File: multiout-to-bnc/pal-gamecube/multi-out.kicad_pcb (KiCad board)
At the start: 2 copper layers, 18.4 x 12 mm, 16 parts, among them U1 AV-CONNECTOR, U2 LM1881

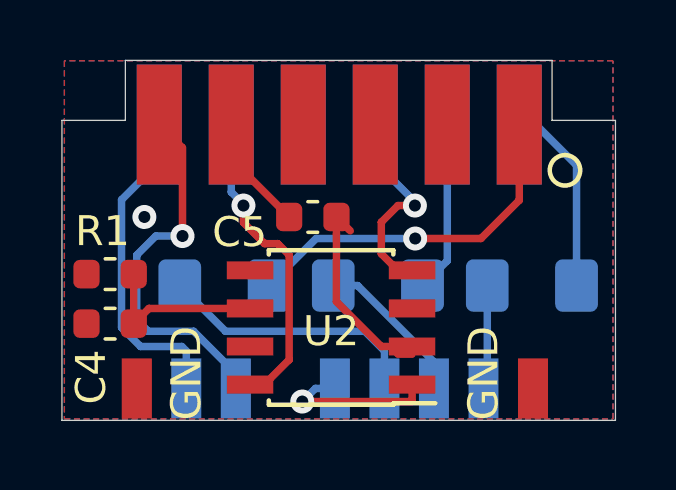
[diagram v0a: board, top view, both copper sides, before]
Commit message: Add 75 Ohm resistor between composite line and ground
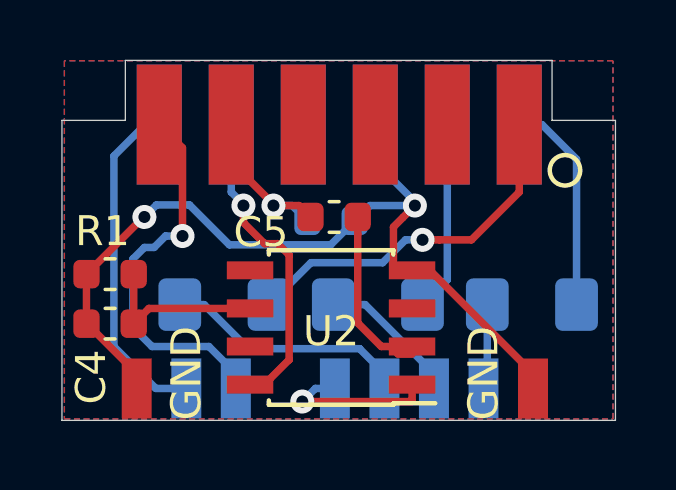
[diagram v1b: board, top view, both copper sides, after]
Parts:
- added R2: 75k, Resistor_SMD:R_0603_1608Metric, B.Cu at (149.0, 109.3)
- moved C5 0.71 mm to (149.1, 109.2)
- moved C1 0.64 mm to (145.4, 112.1)
- moved C2 0.64 mm to (155.7, 112.1)
- moved C3 0.64 mm to (150.5, 112.1)
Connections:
- U1 pad 3: (no net) -> Net-(U1-Pad3)
- U1 pad 7: (no net) -> Net-(U1-Pad7)
- U1 pad 8: (no net) -> Net-(U1-Pad8)
- U2 pad 3: (no net) -> Net-(U2-Pad3)
- U2 pad 5: (no net) -> Net-(U2-Pad5)
- U2 pad 7: (no net) -> Net-(U2-Pad7)
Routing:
- net GND: track 6.90 -> 29.7 mm
- net Net-(C1-Pad1): track 13.3 -> 12.1 mm
- net Net-(C5-Pad2): track 7.09 -> 6.14 mm
- net Net-(C5-Pad1): track 5.13 -> 6.02 mm, vias 0 -> 1
- net Net-(C2-Pad1): track 6.48 -> 7.23 mm
- net Net-(C1-Pad2): track 8.97 -> 8.27 mm
- net Net-(C3-Pad1): track 5.71 -> 6.34 mm
- net Net-(C2-Pad2): track 3.48 -> 2.85 mm
